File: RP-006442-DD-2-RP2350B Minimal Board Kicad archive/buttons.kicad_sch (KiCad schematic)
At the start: 0 parts

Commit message: Update buttons.kicad_sch
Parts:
- added SW5: SW_Omron_B3FS, Button_Switch_SMD:SW_SPST_Omron_B3FS-100xP, symbol Switch:SW_Omron_B3FS
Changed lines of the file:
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@@
 	(generator_version "9.0")
 	(paper "A4")
+	(symbol
+		(lib_id "Switch:SW_Omron_B3FS")
+		(at 152.4 101.6 0)
+		(unit 1)
+		(exclude_from_sim no)
+		(in_bom yes)
+		(on_board yes)
+		(dnp no)
+		(fields_autoplaced yes)
+		(property "Reference" "SW5"
+			(at 152.4 93.98 0)
+			(effects
+				(font
+					(size 1.27 1.27)
+				)
+			)
+		)
+		(property "Value" "SW_Omron_B3FS"
+			(at 152.4 96.52 0)
+			(effects
+				(font
+					(size 1.27 1.27)
+				)
+			)
+		)
+		(property "Footprint" "Button_Switch_SMD:SW_SPST_Omron_B3FS-100xP"
+			(at 152.4 96.52 0)
+			(effects
+				(font
+					(size 1.27 1.27)
+				)
+				(hide yes)
+			)
+		)
+		(property "Datasheet" "https://omronfs.omron.com/en_US/ecb/products/pdf/en-b3fs.pdf"
+			(at 152.4 96.52 0)
+			(effects
+				(font
+					(size 1.27 1.27)
+				)
+				(hide yes)
+			)
+		)
+		(property "Description" "Omron B3FS 6x6mm single pole normally-open tactile switch"
+			(at 152.4 101.6 0)
+			(effects
+				(font
+					(size 1.27 1.27)
+				)
+				(hide yes)
+			)
+		)
+		(pin "2"
+		)
+		(pin "1"
+		)
+		(instances
+			(project ""
+				(path "/94683f5c-9cd9-448e-be96-9792537b5cb8/ba1de432-0703-49aa-92c9-1bafe9390a02"
+					(reference "SW5")
+					(unit 1)
+				)
+			)
+		)
+	)
 )

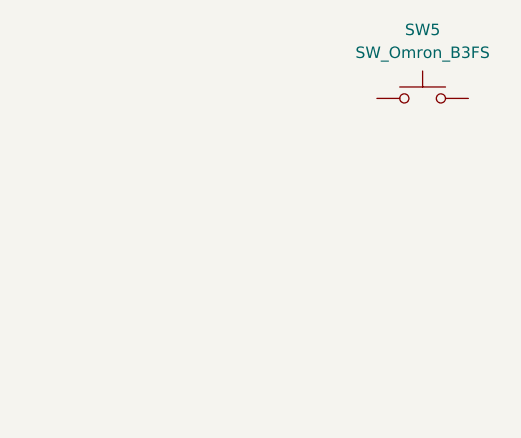
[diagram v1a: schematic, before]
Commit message: Update buttons.kicad_sch
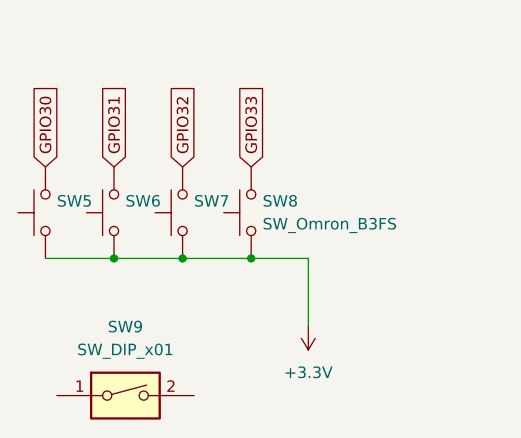
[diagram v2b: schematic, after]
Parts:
- added SW6, SW7, SW8: SW_Omron_B3FS, Button_Switch_SMD:SW_SPST_Omron_B3FS-100xP, symbol Switch:SW_Omron_B3FS
- added SW9: SW_DIP_x01, Button_Switch_SMD:SW_DIP_SPSTx01_Slide_9.78x4.72mm_W8.61mm_P2.54mm, symbol Switch:SW_DIP_x01
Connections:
- net +3.3V: now reaches SW5.1
- net +3.3V: now also SW6.1, SW7.1, SW8.1
- net GPIO30: now reaches SW5.2
- new net GPIO31: SW6.2
- new net GPIO32: SW7.2
- new net GPIO33: SW8.2
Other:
- moved on the sheet: SW5

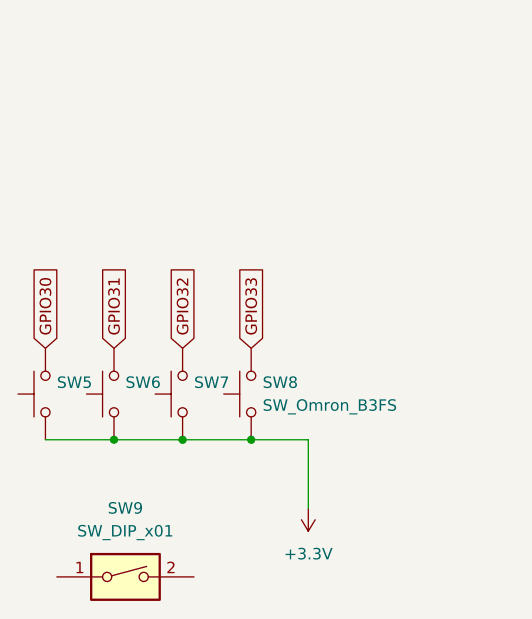
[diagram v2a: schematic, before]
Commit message: Update buttons.kicad_sch
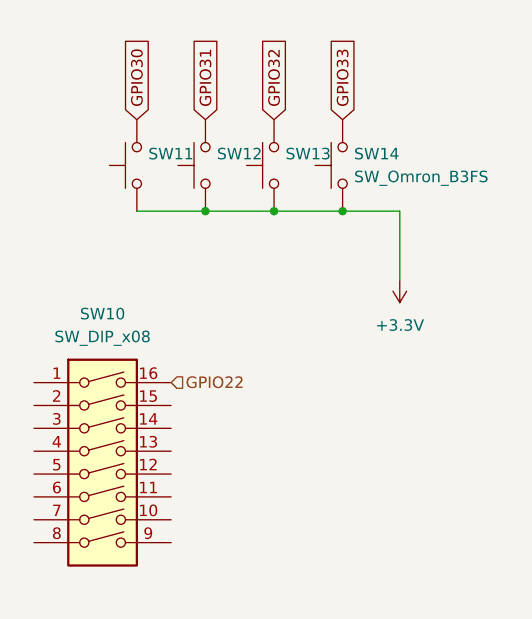
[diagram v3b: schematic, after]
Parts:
- removed SW5, SW6, SW7, SW8: SW_Omron_B3FS, Button_Switch_SMD:SW_SPST_Omron_B3FS-100xP, symbol Switch:SW_Omron_B3FS
- removed SW9: SW_DIP_x01, Button_Switch_SMD:SW_DIP_SPSTx01_Slide_9.78x4.72mm_W8.61mm_P2.54mm, symbol Switch:SW_DIP_x01
- added SW10: SW_DIP_x08, symbol Switch:SW_DIP_x08
- added SW11, SW12, SW13, SW14: SW_Omron_B3FS, Button_Switch_SMD:SW_SPST_Omron_B3FS-100xP, symbol Switch:SW_Omron_B3FS
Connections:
- net +3.3V: now also SW11.1, SW12.1, SW13.1, SW14.1
- net GPIO30: now also SW11.2
- net GPIO31: now also SW12.2
- net GPIO32: now also SW13.2
- net GPIO33: now also SW14.2
- new net GPIO22: SW10.16

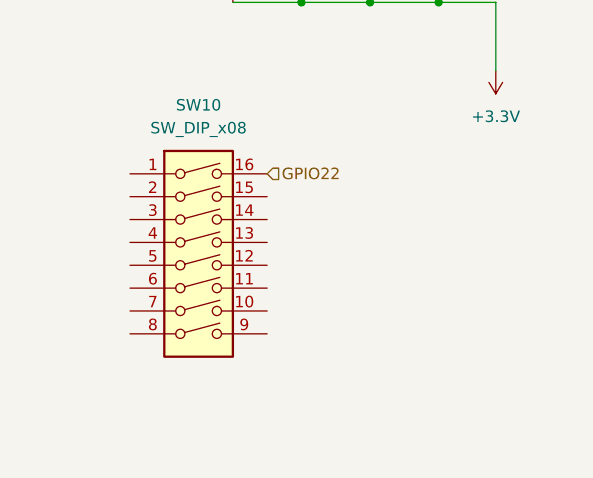
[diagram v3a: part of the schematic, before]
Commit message: Swith buttons added 22*11mm
Button_Switch_SMD:SW_DIP_SPSTx08_Slide_Omron_A6S-810x_W8.9mm_P2.54mm
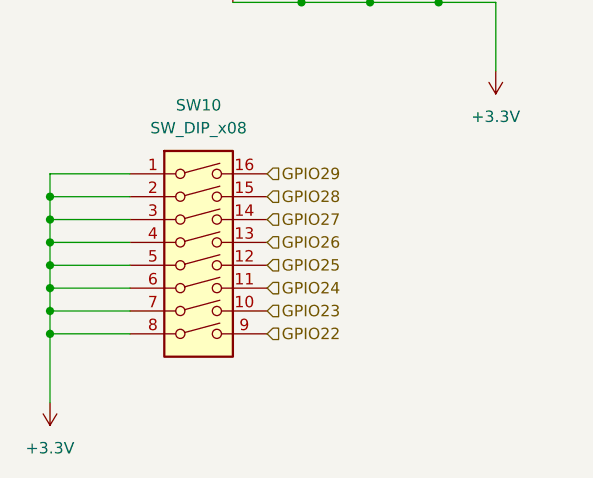
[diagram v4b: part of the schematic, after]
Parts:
- SW10: footprint (none) -> Button_Switch_SMD:SW_DIP_SPSTx08_Slide_Omron_A6S-810x_W8.9mm_P2.54mm
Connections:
- net +3.3V: now also SW10.1, SW10.2, SW10.3, SW10.4, SW10.5, SW10.6, SW10.7, SW10.8
- net GPIO22: now also SW10.9; no longer SW10.16
- net GPIO23: now reaches SW10.10
- net GPIO24: now reaches SW10.11
- net GPIO25: now reaches SW10.12
- net GPIO26: now reaches SW10.13
- net GPIO27: now reaches SW10.14
- net GPIO28: now reaches SW10.15
- new net GPIO29: SW10.16

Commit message: text
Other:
- note added: "DongGuan KINGTEK Industrial Co.,LTD 8-bit SPST Black Flat Toggle, Raised Style SMD-16P,6x20.3mm DIP Switches ROHS"
- note added: "Korean Hroparts Elec 6mm 4.3mm Round Button 50mA Standing paste 6mm SPST 100MΩ 100000 Times 250gf 12V SMD Tactile Switches ROHS"
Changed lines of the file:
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@@
 	(generator_version "9.0")
 	(paper "A4")
+	(text "\nDongGuan KINGTEK Industrial Co.,LTD\n8-bit SPST Black Flat Toggle, \nRaised Style SMD-16P,6x20.3mm DIP Switches ROHS"
+		(exclude_from_sim no)
+		(at 132.08 137.16 0)
+		(effects
+			(font
+				(size 1.27 1.27)
+			)
+		)
+	)
+	(text "\nKorean Hroparts Elec\n6mm 4.3mm Round Button 50mA Standing paste \n6mm SPST 100MΩ 100000 Times 250gf 12V \nSMD Tactile Switches ROHS"
+		(exclude_from_sim no)
+		(at 128.27 97.79 0)
+		(effects
+			(font
+				(size 1.27 1.27)
+			)
+		)
+	)
 	(junction
 		(at 100.33 118.11)
@@
 			)
 		)
-		(property "Datasheet" "~"
+		(property "Datasheet" "https://jlcpcb.com/api/file/downloadByFileSystemAccessId/8588905267774042112"
 			(at 116.84 123.19 0)
 			(effects

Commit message: Update
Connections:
- net GPIO30: now also SW11.1; no longer SW11.2
- net GPIO31: now also SW12.1; no longer SW12.2
- net GPIO32: now also SW13.1; no longer SW13.2
- net GPIO33: now also SW14.1; no longer SW14.2
- net +3.3V renamed GND
- net GND: now also SW11.2, SW12.2, SW13.2, SW14.2; no longer SW11.1, SW12.1, SW13.1, SW14.1
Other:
- note added: "RP2350 configured with internal pull-up resistor"
- moved on the sheet: SW10, SW11, SW12, SW13, SW14

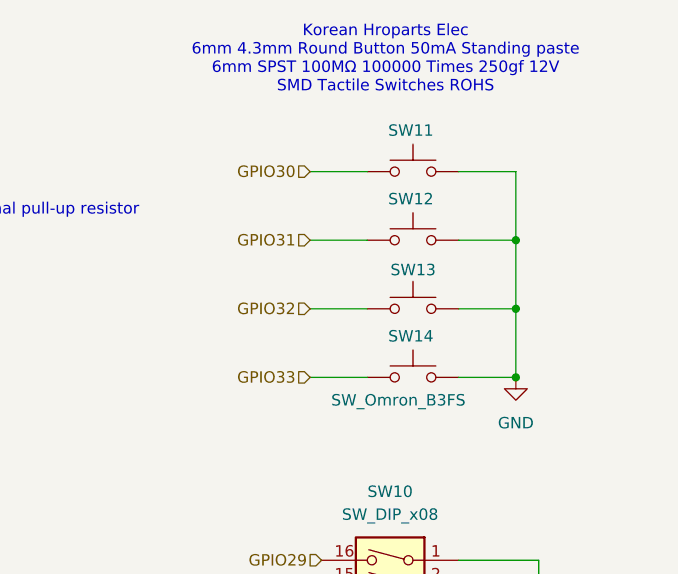
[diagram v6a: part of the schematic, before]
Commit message: Update pushbutton footprints on pcb
Changed from omron pushbutton footprints to custom footprints for JLCPCB part
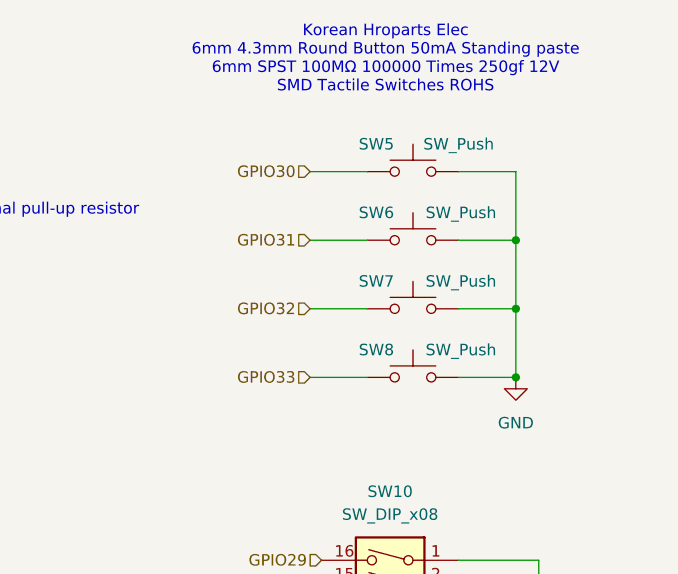
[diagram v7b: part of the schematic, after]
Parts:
- removed SW11, SW12, SW13, SW14: SW_Omron_B3FS, Button_Switch_SMD:SW_SPST_Omron_B3FS-100xP, symbol Switch:SW_Omron_B3FS
- added SW5, SW6, SW7, SW8: SW_Push, Button_Switch_SMD:SW_Push_K2-1102SP-A4SC-04, symbol Switch:SW_Push
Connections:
- net GND: now also SW5.2, SW6.2, SW7.2, SW8.2
- net GPIO30: now also SW5.1
- net GPIO31: now also SW6.1
- net GPIO32: now also SW7.1
- net GPIO33: now also SW8.1
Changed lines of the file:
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@@
 	)
 	(symbol
-		(lib_id "Switch:SW_Omron_B3FS")
+		(lib_id "Switch:SW_Push")
+		(at 138.43 78.74 0)
+		(unit 1)
+		(exclude_from_sim no)
+		(in_bom yes)
+		(on_board yes)
+		(dnp no)
+		(property "Reference" "SW8"
+			(at 134.366 75.692 0)
+			(effects
+				(font
+					(size 1.27 1.27)
+				)
+			)
+		)
+		(property "Value" "SW_Push"
+			(at 143.764 75.692 0)
+			(effects
+				(font
+					(size 1.27 1.27)
+				)
+			)
+		)
+		(property "Footprint" "Button_Switch_SMD:SW_Push_K2-1102SP-A4SC-04"
+			(at 138.43 73.66 0)
+			(effects
+				(font
+					(size 1.27 1.27)
+				)
+				(hide yes)
+			)
+		)
+		(property "Datasheet" "~"
+			(at 138.43 73.66 0)
+			(effects
+				(font
+					(size 1.27 1.27)
+				)
+				(hide yes)
+			)
+		)
+		(property "Description" "Push button switch, generic, two pins"
+			(at 138.43 78.74 0)
+			(effects
+				(font
+					(size 1.27 1.27)
+				)
+				(hide yes)
+			)
+		)
+		(pin "1"
+		)
+		(pin "2"
+		)
+		(instances
+			(project "RP2350_80QFN_minimal"
+				(path "/94683f5c-9cd9-448e-be96-9792537b5cb8/ba1de432-0703-49aa-92c9-1bafe9390a02"
+					(reference "SW8")
+					(unit 1)
+				)
+			)
+		)
+	)
+	(symbol
+		(lib_id "Switch:SW_Push")
 		(at 138.43 55.88 0)
 		(unit 1)
@@
 		(on_board yes)
 		(dnp no)
-		(property "Reference" "SW11"
-			(at 140.716 51.308 0)
-			(effects
-				(font
-					(size 1.27 1.27)
-				)
-				(justify right)
-			)
-		)
-		(property "Value" "SW_Omron_B3FS"
-			(at 137.1601 57.15 90)
-			(effects
-				(font
-					(size 1.27 1.27)
-				)
-				(justify right)
-				(hide yes)
-			)
-		)
-		(property "Footprint" "Button_Switch_SMD:SW_SPST_Omron_B3FS-100xP"
+		(property "Reference" "SW5"
+			(at 134.366 52.832 0)
+			(effects
+				(font
+					(size 1.27 1.27)
+				)
+			)
+		)
+		(property "Value" "SW_Push"
+			(at 143.51 52.832 0)
+			(effects
+				(font
+					(size 1.27 1.27)
+				)
+			)
+		)
+		(property "Footprint" "Button_Switch_SMD:SW_Push_K2-1102SP-A4SC-04"
 			(at 138.43 50.8 0)
 			(effects
@@
 			)
 		)
-		(property "Datasheet" "https://omronfs.omron.com/en_US/ecb/products/pdf/en-b3fs.pdf"
+		(property "Datasheet" "~"
 			(at 138.43 50.8 0)
 			(effects
@@
 			)
 		)
-		(property "Description" "Omron B3FS 6x6mm single pole normally-open tactile switch"
+		(property "Description" "Push button switch, generic, two pins"
 			(at 138.43 55.88 0)
 			(effects
@@
 			)
 		)
+		(pin "1"
+		)
 		(pin "2"
 		)
-		(pin "1"
-		)
-		(instances
-			(project "RP2350_80QFN_minimal"
-				(path "/94683f5c-9cd9-448e-be96-9792537b5cb8/ba1de432-0703-49aa-92c9-1bafe9390a02"
-					(reference "SW11")
+		(instances
+			(project ""
+				(path "/94683f5c-9cd9-448e-be96-9792537b5cb8/ba1de432-0703-49aa-92c9-1bafe9390a02"
+					(reference "SW5")
 					(unit 1)
 				)
@@
 	)
 	(symbol
-		(lib_id "Switch:SW_Omron_B3FS")
+		(lib_id "Switch:SW_Push")
 		(at 138.43 63.5 0)
 		(unit 1)
@@
 		(on_board yes)
 		(dnp no)
-		(property "Reference" "SW12"
-			(at 140.716 58.928 0)
-			(effects
-				(font
-					(size 1.27 1.27)
-				)
-				(justify right)
-			)
-		)
-		(property "Value" "SW_Omron_B3FS"
-			(at 137.1601 64.77 90)
-			(effects
-				(font
-					(size 1.27 1.27)
-				)
-				(justify right)
-				(hide yes)
-			)
-		)
-		(property "Footprint" "Button_Switch_SMD:SW_SPST_Omron_B3FS-100xP"
+		(property "Reference" "SW6"
+			(at 134.366 60.452 0)
+			(effects
+				(font
+					(size 1.27 1.27)
+				)
+			)
+		)
+		(property "Value" "SW_Push"
+			(at 143.764 60.452 0)
+			(effects
+				(font
+					(size 1.27 1.27)
+				)
+			)
+		)
+		(property "Footprint" "Button_Switch_SMD:SW_Push_K2-1102SP-A4SC-04"
 			(at 138.43 58.42 0)
 			(effects
@@
 			)
 		)
-		(property "Datasheet" "https://omronfs.omron.com/en_US/ecb/products/pdf/en-b3fs.pdf"
+		(property "Datasheet" "~"
 			(at 138.43 58.42 0)
 			(effects
@@
 			)
 		)
-		(property "Description" "Omron B3FS 6x6mm single pole normally-open tactile switch"
+		(property "Description" "Push button switch, generic, two pins"
 			(at 138.43 63.5 0)
 			(effects
@@
 			)
 		)
+		(pin "1"
+		)
 		(pin "2"
 		)
-		(pin "1"
-		)
 		(instances
 			(project "RP2350_80QFN_minimal"
 				(path "/94683f5c-9cd9-448e-be96-9792537b5cb8/ba1de432-0703-49aa-92c9-1bafe9390a02"
-					(reference "SW12")
+					(reference "SW6")
 					(unit 1)
 				)
@@
 	)
 	(symbol
-		(lib_id "Switch:SW_Omron_B3FS")
+		(lib_id "Switch:SW_Push")
 		(at 138.43 71.12 0)
 		(unit 1)
@@
 		(on_board yes)
 		(dnp no)
-		(property "Reference" "SW13"
-			(at 140.97 66.802 0)
-			(effects
-				(font
-					(size 1.27 1.27)
-				)
-				(justify right)
-			)
-		)
-		(property "Value" "SW_Omron_B3FS"
-			(at 137.1601 72.39 90)
-			(effects
-				(font
-					(size 1.27 1.27)
-				)
-				(justify right)
-				(hide yes)
-			)
-		)
-		(property "Footprint" "Button_Switch_SMD:SW_SPST_Omron_B3FS-100xP"
+		(property "Reference" "SW7"
+			(at 134.366 68.072 0)
+			(effects
+				(font
+					(size 1.27 1.27)
+				)
+			)
+		)
+		(property "Value" "SW_Push"
+			(at 143.764 68.072 0)
+			(effects
+				(font
+					(size 1.27 1.27)
+				)
+			)
+		)
+		(property "Footprint" "Button_Switch_SMD:SW_Push_K2-1102SP-A4SC-04"
 			(at 138.43 66.04 0)
 			(effects
@@
 			)
 		)
-		(property "Datasheet" "https://omronfs.omron.com/en_US/ecb/products/pdf/en-b3fs.pdf"
+		(property "Datasheet" "~"
 			(at 138.43 66.04 0)
 			(effects
@@
 			)
 		)
-		(property "Description" "Omron B3FS 6x6mm single pole normally-open tactile switch"
+		(property "Description" "Push button switch, generic, two pins"
 			(at 138.43 71.12 0)
 			(effects
@@
 			)
 		)
+		(pin "1"
+		)
 		(pin "2"
 		)
-		(pin "1"
-		)
 		(instances
 			(project "RP2350_80QFN_minimal"
 				(path "/94683f5c-9cd9-448e-be96-9792537b5cb8/ba1de432-0703-49aa-92c9-1bafe9390a02"
-					(reference "SW13")
-					(unit 1)
-				)
-			)
-		)
-	)
-	(symbol
-		(lib_id "Switch:SW_Omron_B3FS")
-		(at 138.43 78.74 0)
-		(unit 1)
-		(exclude_from_sim no)
-		(in_bom yes)
-		(on_board yes)
-		(dnp no)
-		(property "Reference" "SW14"
-			(at 140.716 74.168 0)
-			(effects
-				(font
-					(size 1.27 1.27)
-				)
-				(justify right)
-			)
-		)
-		(property "Value" "SW_Omron_B3FS"
-			(at 144.272 81.28 0)
-			(effects
-				(font
-					(size 1.27 1.27)
-				)
-				(justify right)
-			)
-		)
-		(property "Footprint" "Button_Switch_SMD:SW_SPST_Omron_B3FS-100xP"
-			(at 138.43 73.66 0)
-			(effects
-				(font
-					(size 1.27 1.27)
-				)
-				(hide yes)
-			)
-		)
-		(property "Datasheet" "https://omronfs.omron.com/en_US/ecb/products/pdf/en-b3fs.pdf"
-			(at 138.43 73.66 0)
-			(effects
-				(font
-					(size 1.27 1.27)
-				)
-				(hide yes)
-			)
-		)
-		(property "Description" "Omron B3FS 6x6mm single pole normally-open tactile switch"
-			(at 138.43 78.74 0)
-			(effects
-				(font
-					(size 1.27 1.27)
-				)
-				(hide yes)
-			)
-		)
-		(pin "2"
-		)
-		(pin "1"
-		)
-		(instances
-			(project "RP2350_80QFN_minimal"
-				(path "/94683f5c-9cd9-448e-be96-9792537b5cb8/ba1de432-0703-49aa-92c9-1bafe9390a02"
-					(reference "SW14")
-					(unit 1)
-				)
+					(reference "SW7")
+					(unit 1)
+				)

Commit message: Big update
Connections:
- net GPIO22: now also SW10.16; no longer SW10.9
- net GPIO23: now also SW10.15; no longer SW10.10
- net GPIO24: now also SW10.14; no longer SW10.11
- net GPIO25: now also SW10.13; no longer SW10.12
- net GPIO26: now also SW10.12; no longer SW10.13
- net GPIO27: now also SW10.11; no longer SW10.14
- net GPIO28: now also SW10.10; no longer SW10.15
- net GPIO29: now also SW10.9; no longer SW10.16
